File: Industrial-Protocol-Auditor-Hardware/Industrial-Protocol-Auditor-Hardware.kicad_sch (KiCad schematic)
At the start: 81 parts, among them J1 USB_C_Receptacle, J2 Conn_01x08, J3 CAN_Port, J4 RS_Port, J5 Jack-DC, J6 Batt_Port, M1 Motor_DC, Q1 Q_NMOS, SW1 RST, SW2 BOOT, SW3 UP, SW4 DOWN, SW5 LEFT, SW6 RIGHT, SW7 OK, SW8 SW_SPDT, U1 ESP32-S3-WROOM-1, U2 MAX3485, U3 SN65HVD230, U4 DS3231MZ, U5 W25Q16JVSS, U6 LM2596S-5, U8 BQ24074RGT, U9 TPS63001

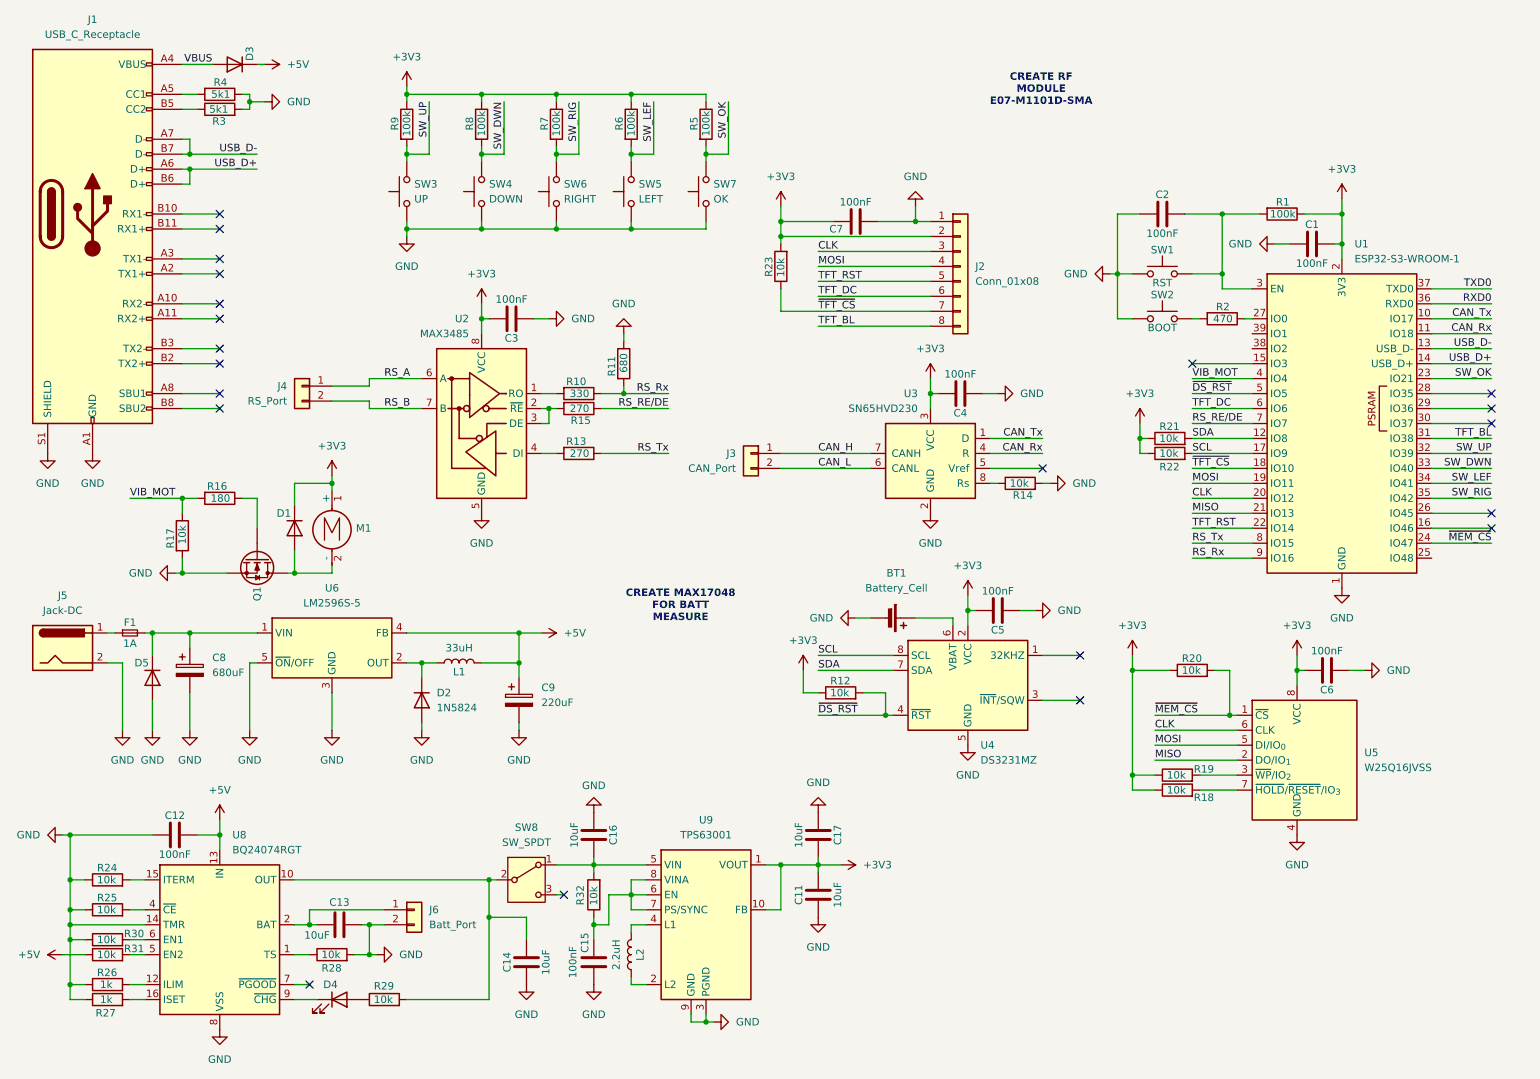
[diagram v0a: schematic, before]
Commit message: Populated all footprints and Component LCSC Reference. Started the board design.
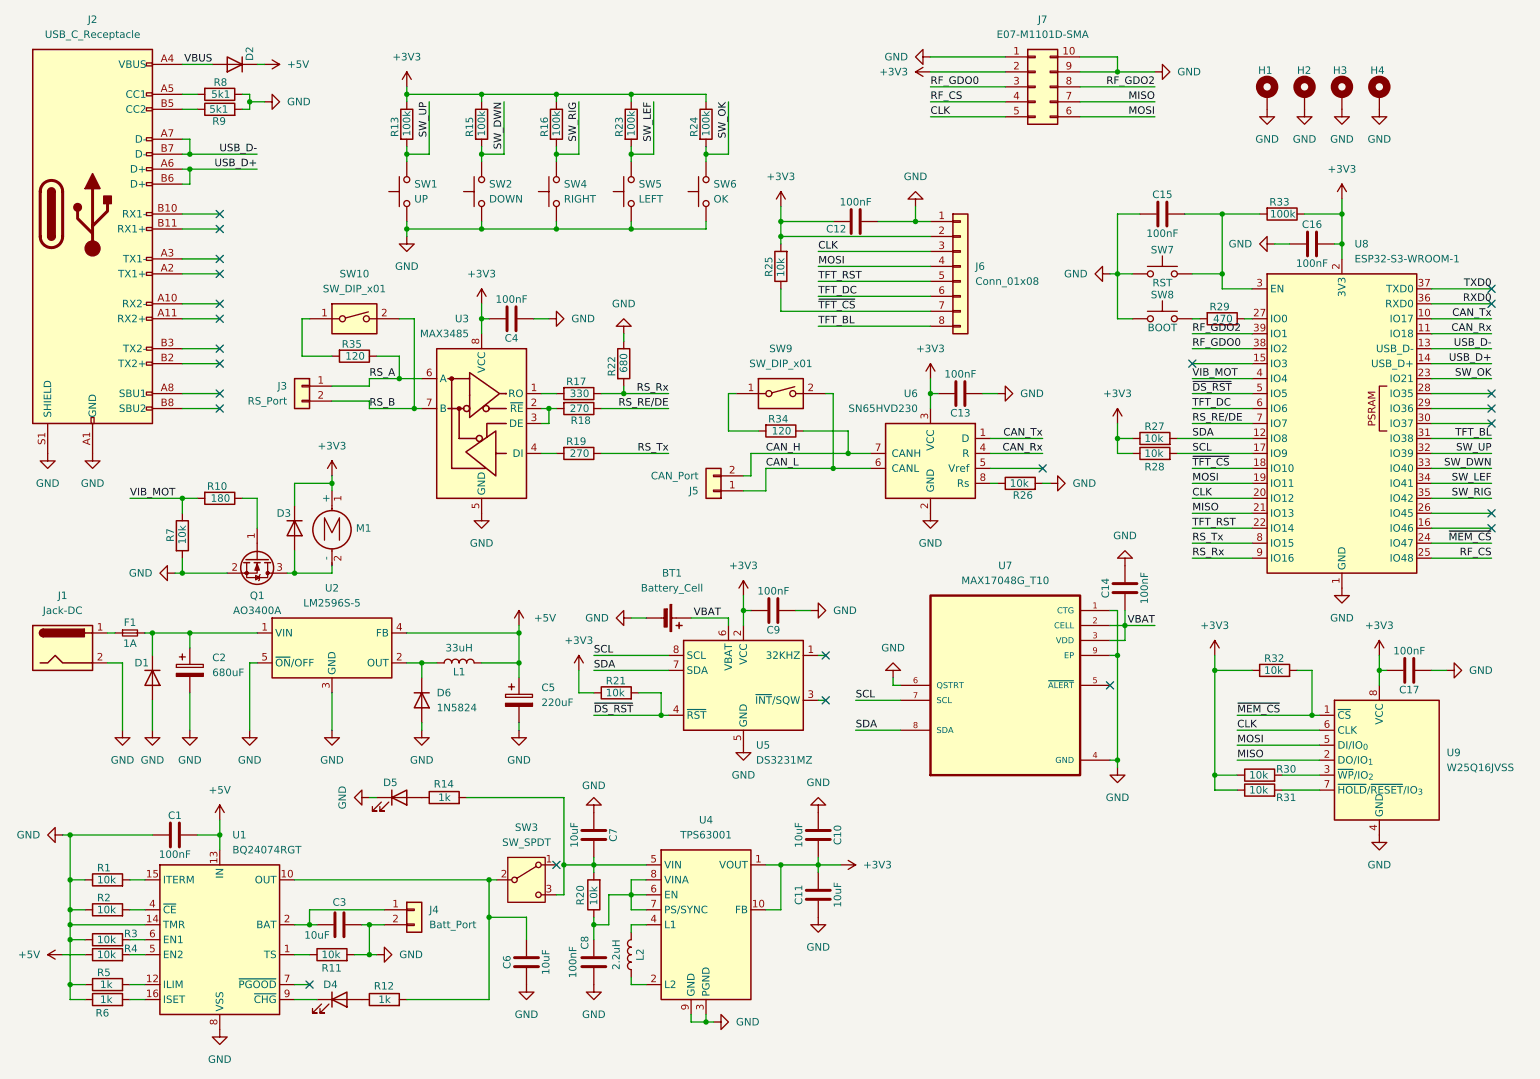
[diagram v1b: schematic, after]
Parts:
- removed Q1: Q_NMOS, symbol Device:Q_NMOS
- added C14: 100nF, Capacitor_SMD:C_0603_1608Metric, symbol Device:C
- added D5: LED, LED_SMD:LED_0603_1608Metric, symbol Device:LED
- added H1, H2, H3, H4: MountingHole_Pad, MountingHole:MountingHole_2.7mm_M2.5, symbol Mechanical:MountingHole_Pad
- added J7: E07-M1101D-SMA, Connector_PinHeader_2.54mm:PinHeader_2x05_P2.54mm_Vertical, symbol Connector_Generic:Conn_02x05_Counter_Clockwise
- added Q1: AO3400A, Package_TO_SOT_SMD:SOT-23, symbol Transistor_FET:AO3400A
- added R14: 1k, Resistor_SMD:R_0603_1608Metric, symbol Device:R
- added R34, R35: 120, Resistor_SMD:R_0603_1608Metric, symbol Device:R
- added SW10, SW9: SW_DIP_x01, Button_Switch_SMD:SW_DIP_SPSTx01_Slide_6.7x4.1mm_W6.73mm_P2.54mm_LowProfile_JPin, symbol Switch:SW_DIP_x01
- added U7: MAX17048G_T10, Package_DFN_QFN:DFN-8-1EP_2x2mm_P0.5mm_EP0.8x1.6mm, symbol MAX17048G_T10:MAX17048G_T10
- BT1: footprint (none) -> Battery:BatteryHolder_LINX_BAT-HLD-012-SMT; LCSC Part (none) -> C964817; Price (none) -> 0.0989
- C1: renamed from C12; footprint (none) -> Capacitor_SMD:C_0603_1608Metric; LCSC Part (none) -> C14663; Price (none) -> 0.0024
- C10: renamed from C17; footprint (none) -> Capacitor_SMD:C_0603_1608Metric; LCSC Part (none) -> C19702; Price (none) -> 0.0056
- C11: footprint (none) -> Capacitor_SMD:C_0603_1608Metric; LCSC Part (none) -> C19702; Price (none) -> 0.0056
- C12: renamed from C7; footprint (none) -> Capacitor_SMD:C_0603_1608Metric; LCSC Part (none) -> C14663; Price (none) -> 0.0024
- C13: renamed from C4; footprint (none) -> Capacitor_SMD:C_0603_1608Metric; LCSC Part (none) -> C14663; Price (none) -> 0.0024
- C15: renamed from C2; footprint (none) -> Capacitor_SMD:C_0603_1608Metric; LCSC Part (none) -> C14663; Price (none) -> 0.0024
- C16: renamed from C1; footprint (none) -> Capacitor_SMD:C_0603_1608Metric; LCSC Part (none) -> C14663; Price (none) -> 0.0024
- C17: renamed from C6; footprint (none) -> Capacitor_SMD:C_0603_1608Metric; LCSC Part (none) -> C14663; Price (none) -> 0.0024
- C2: renamed from C8; footprint (none) -> Capacitor_SMD:CP_Elec_10x10.5; LCSC Part (none) -> C2983320; Price (none) -> 0.0905
- C3: renamed from C13; footprint (none) -> Capacitor_SMD:C_0603_1608Metric; LCSC Part (none) -> C19702; Price (none) -> 0.0056
- C4: renamed from C3; footprint (none) -> Capacitor_SMD:C_0603_1608Metric; LCSC Part (none) -> C14663; Price (none) -> 0.0024
- C5: renamed from C9; footprint (none) -> Capacitor_SMD:CP_Elec_6.3x7.7; LCSC Part (none) -> C2887273; Price (none) -> 0.0345
- C6: renamed from C14; footprint (none) -> Capacitor_SMD:C_0603_1608Metric; LCSC Part (none) -> C19702; Price (none) -> 0.0056
- C7: renamed from C16; footprint (none) -> Capacitor_SMD:C_0603_1608Metric; LCSC Part (none) -> C19702; Price (none) -> 0.0056
- C8: renamed from C15; footprint (none) -> Capacitor_SMD:C_0603_1608Metric; LCSC Part (none) -> C14663; Price (none) -> 0.0024
- C9: renamed from C5; footprint (none) -> Capacitor_SMD:C_0603_1608Metric; LCSC Part (none) -> C14663; Price (none) -> 0.0024
- D1: renamed from D5; value D -> 1N5824; footprint (none) -> Diode_SMD:D_SMA; LCSC Part (none) -> C8678; Price (none) -> 0.0276
- D2: renamed from D3; value D -> 1N5824; footprint (none) -> Diode_SMD:D_SMA; LCSC Part (none) -> C8678; Price (none) -> 0.0276
- D3: renamed from D1; value D -> 1N5824; footprint (none) -> Diode_SMD:D_SMA; LCSC Part (none) -> C8678; Price (none) -> 0.0276
- D4: footprint (none) -> LED_SMD:LED_0603_1608Metric; LCSC Part (none) -> C2286; Price (none) -> 0.0056
- D6: renamed from D2; footprint (none) -> Diode_SMD:D_SMA; LCSC Part (none) -> C8678; Price (none) -> 0.0276
- F1: footprint (none) -> Fuse:Fuse_1206_3216Metric; LCSC Part (none) -> C720075; Price (none) -> 0.0297
- J1: renamed from J5; footprint (none) -> Connector_BarrelJack:BarrelJack_Horizontal; LCSC Part (none) -> C16214; Price (none) -> 0.0530
- J2: renamed from J1; footprint (none) -> Connector_USB:USB_C_Receptacle_GCT_USB4105-xx-A_16P_TopMnt_Horizontal; LCSC Part (none) -> C393939; Price (none) -> 0.0644
- J3: renamed from J4; footprint (none) -> TerminalBlock:TerminalBlock_MaiXu_MX126-5.0-02P_1x02_P5.00mm; LCSC Part (none) -> C474881; Price (none) -> 0.0839
- J4: renamed from J6; footprint (none) -> Connector_JST:JST_XH_S2B-XH-A_1x02_P2.50mm_Horizontal; LCSC Part (none) -> C157931; Price (none) -> 0.0738
- J5: renamed from J3; footprint (none) -> TerminalBlock:TerminalBlock_MaiXu_MX126-5.0-02P_1x02_P5.00mm; LCSC Part (none) -> C474881; Price (none) -> 0.0839
- J6: renamed from J2; footprint (none) -> Connector_JST:JST_XH_S8B-XH-A_1x08_P2.50mm_Horizontal; LCSC Part (none) -> C157914; Price (none) -> 0.1645
- L1: footprint (none) -> Inductor_SMD:L_Chilisin_BMRF00101040; LCSC Part (none) -> C6364680; Price (none) -> 0.2336
- L2: footprint (none) -> Inductor_SMD:L_1008_2520Metric; LCSC Part (none) -> C86092; Price (none) -> 0.0629
- M1: footprint (none) -> Connector_PinHeader_2.54mm:PinHeader_1x02_P2.54mm_Vertical; LCSC Part (none) -> -; Price (none) -> -
- R1: renamed from R24; footprint (none) -> Resistor_SMD:R_0603_1608Metric; LCSC Part (none) -> C25804; Price (none) -> 0.0009
- R10: renamed from R16; footprint (none) -> Resistor_SMD:R_0603_1608Metric; LCSC Part (none) -> C2907000; Price (none) -> 0.0009
- R11: renamed from R28; footprint (none) -> Resistor_SMD:R_0603_1608Metric; LCSC Part (none) -> C25804; Price (none) -> 0.0009
- R12: renamed from R29; value 10k -> 1k; footprint (none) -> Resistor_SMD:R_0603_1608Metric; LCSC Part (none) -> C21190; Price (none) -> 0.0010
- R13: renamed from R9; footprint (none) -> Resistor_SMD:R_0603_1608Metric; LCSC Part (none) -> C25803; Price (none) -> 0.0010
- R15: renamed from R8; footprint (none) -> Resistor_SMD:R_0603_1608Metric; LCSC Part (none) -> C25803; Price (none) -> 0.0010
- R16: renamed from R7; footprint (none) -> Resistor_SMD:R_0603_1608Metric; LCSC Part (none) -> C25803; Price (none) -> 0.0010
- R17: renamed from R10; footprint (none) -> Resistor_SMD:R_0603_1608Metric; LCSC Part (none) -> C23138; Price (none) -> 0.0011
- R18: renamed from R15; footprint (none) -> Resistor_SMD:R_0603_1608Metric; LCSC Part (none) -> C22966; Price (none) -> 0.0011
- R19: renamed from R13; footprint (none) -> Resistor_SMD:R_0603_1608Metric; LCSC Part (none) -> C22966; Price (none) -> 0.0011
- R2: renamed from R25; footprint (none) -> Resistor_SMD:R_0603_1608Metric; LCSC Part (none) -> C25804; Price (none) -> 0.0009
- R20: renamed from R32; footprint (none) -> Resistor_SMD:R_0603_1608Metric; LCSC Part (none) -> C25804; Price (none) -> 0.0009
- R21: renamed from R12; footprint (none) -> Resistor_SMD:R_0603_1608Metric; LCSC Part (none) -> C25804; Price (none) -> 0.0009
- R22: renamed from R11; footprint (none) -> Resistor_SMD:R_0603_1608Metric; LCSC Part (none) -> C23228; Price (none) -> 0.0011
- R23: renamed from R6; footprint (none) -> Resistor_SMD:R_0603_1608Metric; LCSC Part (none) -> C25803; Price (none) -> 0.0010
- R24: renamed from R5; footprint (none) -> Resistor_SMD:R_0603_1608Metric; LCSC Part (none) -> C25803; Price (none) -> 0.0010
- R25: renamed from R23; footprint (none) -> Resistor_SMD:R_0603_1608Metric; LCSC Part (none) -> C25804; Price (none) -> 0.0009
- R26: renamed from R14; footprint (none) -> Resistor_SMD:R_0603_1608Metric; LCSC Part (none) -> C25804; Price (none) -> 0.0009
- R27: renamed from R21; footprint (none) -> Resistor_SMD:R_0603_1608Metric; LCSC Part (none) -> C25804; Price (none) -> 0.0009
- R28: renamed from R22; footprint (none) -> Resistor_SMD:R_0603_1608Metric; LCSC Part (none) -> C25804; Price (none) -> 0.0009
- R29: renamed from R2; footprint (none) -> Resistor_SMD:R_0603_1608Metric; LCSC Part (none) -> C23179; Price (none) -> 0.0011
- R3: renamed from R30; footprint (none) -> Resistor_SMD:R_0603_1608Metric; LCSC Part (none) -> C25804; Price (none) -> 0.0009
- R30: renamed from R19; footprint (none) -> Resistor_SMD:R_0603_1608Metric; LCSC Part (none) -> C25804; Price (none) -> 0.0009
- R31: renamed from R18; footprint (none) -> Resistor_SMD:R_0603_1608Metric; LCSC Part (none) -> C25804; Price (none) -> 0.0009
- R32: renamed from R20; footprint (none) -> Resistor_SMD:R_0603_1608Metric; LCSC Part (none) -> C25804; Price (none) -> 0.0009
- R33: renamed from R1; footprint (none) -> Resistor_SMD:R_0603_1608Metric; LCSC Part (none) -> C25803; Price (none) -> 0.0010
- R4: renamed from R31; footprint (none) -> Resistor_SMD:R_0603_1608Metric; LCSC Part (none) -> C25804; Price (none) -> 0.0009
- R5: renamed from R26; footprint (none) -> Resistor_SMD:R_0603_1608Metric; LCSC Part (none) -> C21190; Price (none) -> 0.0010
- R6: renamed from R27; footprint (none) -> Resistor_SMD:R_0603_1608Metric; LCSC Part (none) -> C21190; Price (none) -> 0.0010
- R7: renamed from R17; footprint (none) -> Resistor_SMD:R_0603_1608Metric; LCSC Part (none) -> C25804; Price (none) -> 0.0009
- R8: renamed from R4; footprint (none) -> Resistor_SMD:R_0603_1608Metric; LCSC Part (none) -> C23186; Price (none) -> 0.0010
- R9: renamed from R3; footprint (none) -> Resistor_SMD:R_0603_1608Metric; LCSC Part (none) -> C23186; Price (none) -> 0.0010
- SW1: renamed from SW3; footprint (none) -> Button_Switch_SMD:SW_SPST_PTS645Sx43SMTR92; LCSC Part (none) -> C19191552; Price (none) -> 0.0621
- SW2: renamed from SW4; footprint (none) -> Button_Switch_SMD:SW_SPST_PTS645Sx43SMTR92; LCSC Part (none) -> C19191552; Price (none) -> 0.0621
- SW3: renamed from SW8; footprint Button_Switch_THT:SW_Slide-03_Wuerth-WS-SLTV_10x2.5x6.4_P2.54mm -> Button_Switch_THT:SW_Slide_SPDT_Angled_CK_OS102011MA1Q; LCSC Part (none) -> C431548; Price (none) -> 0.0215
- SW4: renamed from SW6; footprint (none) -> Button_Switch_SMD:SW_SPST_PTS645Sx43SMTR92; LCSC Part (none) -> C19191552; Price (none) -> 0.0621
- SW5: footprint (none) -> Button_Switch_SMD:SW_SPST_PTS645Sx43SMTR92; LCSC Part (none) -> C19191552; Price (none) -> 0.0621
- SW6: renamed from SW7; footprint (none) -> Button_Switch_SMD:SW_SPST_PTS645Sx43SMTR92; LCSC Part (none) -> C19191552; Price (none) -> 0.0621
- SW7: renamed from SW1; footprint (none) -> Button_Switch_SMD:SW_SPST_PTS645Sx43SMTR92; LCSC Part (none) -> C19191552; Price (none) -> 0.0621
- SW8: renamed from SW2; footprint (none) -> Button_Switch_SMD:SW_SPST_PTS645Sx43SMTR92; LCSC Part (none) -> C19191552; Price (none) -> 0.0621
- U1: renamed from U8; LCSC Part (none) -> C2861252; Price (none) -> 2.8590
- U2: renamed from U6; LCSC Part (none) -> C347421; Price (none) -> 0.5565
- U3: renamed from U2; LCSC Part (none) -> C9943; Price (none) -> 1.4655
- U4: renamed from U9; LCSC Part (none) -> C28060; Price (none) -> 1.1400
- U5: renamed from U4; footprint Package_SO:SOIC-16W_7.5x10.3mm_P1.27mm -> Package_SO:SOIC-8_5.3x5.3mm_P1.27mm; LCSC Part (none) -> C107410; Price (none) -> 2.6325
- U6: renamed from U3; LCSC Part (none) -> C12084; Price (none) -> 0.5010
- U8: renamed from U1; footprint Package_DFN_QFN:QFN-56-1EP_7x7mm_P0.4mm_EP4x4mm -> RF_Module:ESP32-S3-WROOM-1; LCSC Part (none) -> C2913202; Price (none) -> 5.4030
- U9: renamed from U5; LCSC Part (none) -> C82317; Price (none) -> 0.5550
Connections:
- net +3V3: now also J7.2 (Pin_2)
- net CAN_H: now also J5.2 (Pin_2), R34.1; no longer J5.1 (Pin_1)
- net CAN_L: now also J5.1 (Pin_1), SW9.2; no longer J5.2 (Pin_2)
- net CLK: now also J7.5 (Pin_5)
- net GND: now also C14.2, D5.1 (K), H1.1, H2.1, H3.1, H4.1, J7.1 (Pin_1), J7.10 (Pin_10), J7.9 (Pin_9), Q1.2 (S), U7.1 (CTG), U7.4 (GND), U7.6 (QSTRT), U7.9 (EP)
- net MISO: now also J7.7 (Pin_7)
- net MOSI: now also J7.6 (Pin_6)
- net RS_A: now also R35.1
- net RS_B: now also SW10.2
- net SCL: now also U7.7 (SCL)
- net SDA: now also U7.8 (SDA)
- net RF_CS: now reaches U8.25 (IO48)
- net RF_CS: now also J7.4 (Pin_4)
- net RF_GDO0: now reaches U8.38 (IO2)
- net RF_GDO0: now also J7.3 (Pin_3)
- net RF_GDO2: now reaches U8.39 (IO1)
- net RF_GDO2: now also J7.8 (Pin_8)
- net at R10.1: now also Q1.1 (G)
- net VBAT: now reaches BT1.1 (+), U5.6 (VBAT)
- net VBAT: now also C14.1, U7.2 (CELL), U7.3 (VDD)
- net at C7.2, R20.2, U4.5 (VIN): now also SW3.3 (C), R14.2; no longer SW3.1 (A)
- net at D3.2 (A), M1.2 (-): now also Q1.3 (D)
- new net: R35.2, SW10.1
- new net: D5.2 (A), R14.1
- new net: R34.2, SW9.1
- no-connect marks 21 -> 24
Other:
- note removed: "CREATE MAX17048 FOR BATT MEASURE"
- note removed: "CREATE RF MODULE E07-M1101D-SMA"
- moved on the sheet: BT1, C17, C9, J5, R21, R27, R28, R30, R31, R32, U5, U9
